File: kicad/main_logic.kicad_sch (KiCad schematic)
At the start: 15 parts, among them U10 74LS00, U17 28 PIN ZIF, U3 74LS245, U4 74LS244, U5 74LS244, U8 74LS04, U9 74LS08

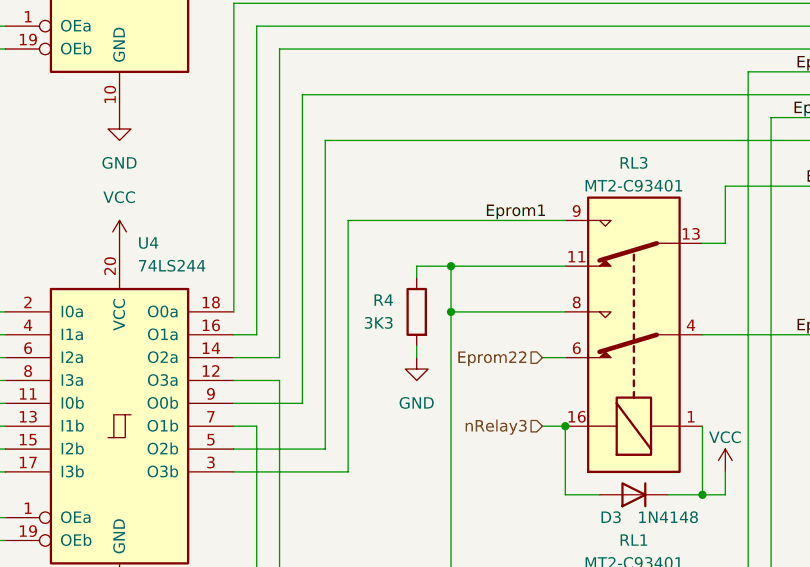
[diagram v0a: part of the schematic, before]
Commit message: KiCAD: larger footprint for 1W resistors
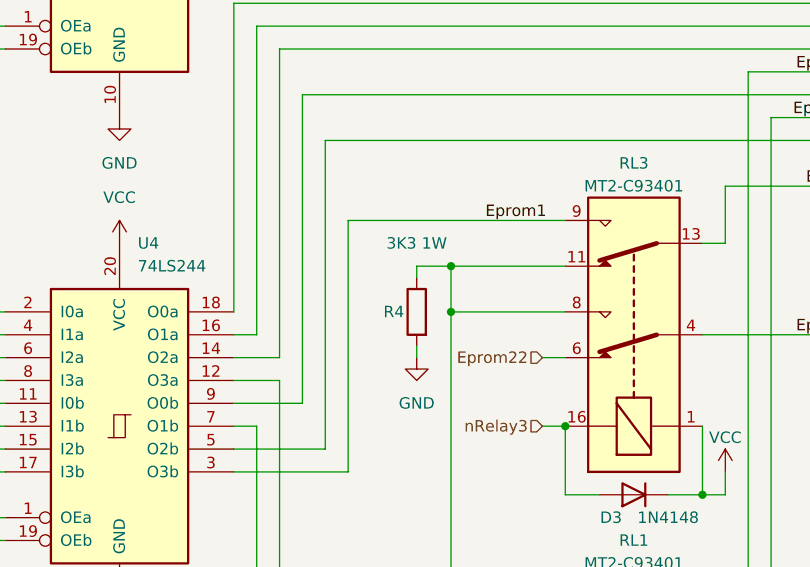
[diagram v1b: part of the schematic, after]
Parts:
- R4: value 3K3 -> 3K3 1W; footprint Resistor_THT:R_Axial_DIN0207_L6.3mm_D2.5mm_P10.16mm_Horizontal -> Resistor_THT:R_Axial_DIN0309_L9.0mm_D3.2mm_P12.70mm_Horizontal
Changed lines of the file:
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@@
   (symbol (lib_id "Device:R") (at 157.48 96.52 0) (mirror y) (unit 1)
     (in_bom yes) (on_board yes)
-    (property "Reference" "R4" (id 0) (at 154.94 95.2499 0)
-      (effects (font (size 1.27 1.27)) (justify left))
-    )
-    (property "Value" "3K3" (id 1) (at 154.94 97.7899 0)
-      (effects (font (size 1.27 1.27)) (justify left))
-    )
-    (property "Footprint" "Resistor_THT:R_Axial_DIN0207_L6.3mm_D2.5mm_P10.16mm_Horizontal" (id 2) (at 159.258 96.52 90)
+    (property "Reference" "R4" (id 0) (at 154.94 96.52 0))
+    (property "Value" "3K3 1W" (id 1) (at 157.48 88.9 0))
+    (property "Footprint" "Resistor_THT:R_Axial_DIN0309_L9.0mm_D3.2mm_P12.70mm_Horizontal" (id 2) (at 159.258 96.52 90)
       (effects (font (size 1.27 1.27)) hide)
     )

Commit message: KiCAD: Make space for full ZIF
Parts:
- R19: footprint custom_footprints:R_Axial_DIN0207_L6.3mm_D2.0mm_P11.43mm_Horizontal -> custom_footprints:R_Axial_DIN0207_L6.3mm_D2.0mm_P10.16mm_Horizontal
- U17: footprint custom_footprints:DIP-28_W15.24mm_Socket_LongPads -> custom_footprints:DIP_Socket-28_W11.9_W12.7_W15.24_W17.78_W18.5_3M_228-1277-00-0602J
- U3, U4, U5: footprint custom_footprints:DIP-20_W7.62mm_Socket -> custom_footprints:DIP-20_W7.62mm_Socket_tweaked
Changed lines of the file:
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@@
       (effects (font (size 1.27 1.27)) (justify left))
     )
-    (property "Footprint" "custom_footprints:DIP-20_W7.62mm_Socket" (id 2) (at 124.46 54.61 0)
+    (property "Footprint" "custom_footprints:DIP-20_W7.62mm_Socket_tweaked" (id 2) (at 124.46 54.61 0)
       (effects (font (size 1.27 1.27)) hide)
     )
@@
       (effects (font (size 1.27 1.27)) (justify left))
     )
-    (property "Footprint" "custom_footprints:DIP-28_W15.24mm_Socket_LongPads" (id 2) (at 222.25 64.77 0)
+    (property "Footprint" "custom_footprints:DIP_Socket-28_W11.9_W12.7_W15.24_W17.78_W18.5_3M_228-1277-00-0602J" (id 2) (at 222.25 64.77 0)
       (effects (font (size 1.27 1.27)) hide)
     )
@@
       (effects (font (size 1.27 1.27)) (justify left))
     )
-    (property "Footprint" "custom_footprints:DIP-20_W7.62mm_Socket" (id 2) (at 256.54 54.61 0)
+    (property "Footprint" "custom_footprints:DIP-20_W7.62mm_Socket_tweaked" (id 2) (at 256.54 54.61 0)
       (effects (font (size 1.27 1.27)) hide)
     )
@@
       (effects (font (size 1.27 1.27)) (justify left))
     )
-    (property "Footprint" "custom_footprints:R_Axial_DIN0207_L6.3mm_D2.0mm_P11.43mm_Horizontal" (id 2) (at 99.822 129.54 90)
+    (property "Footprint" "custom_footprints:R_Axial_DIN0207_L6.3mm_D2.0mm_P10.16mm_Horizontal" (id 2) (at 99.822 129.54 90)
       (effects (font (size 1.27 1.27)) hide)
     )
@@
       (effects (font (size 1.27 1.27)) (justify left))
     )
-    (property "Footprint" "custom_footprints:DIP-20_W7.62mm_Socket" (id 2) (at 124.46 109.22 0)
-      (effects (font (size 1.27 1.27)) hide)
-    )
+    (property "Footprint" "custom_footprints:DIP-20_W7.62mm_Socket_tweaked" (id 2) (at 124.46 109.22 0)
+      (effects (font (size 1.27 1.27)) hide)
+    )

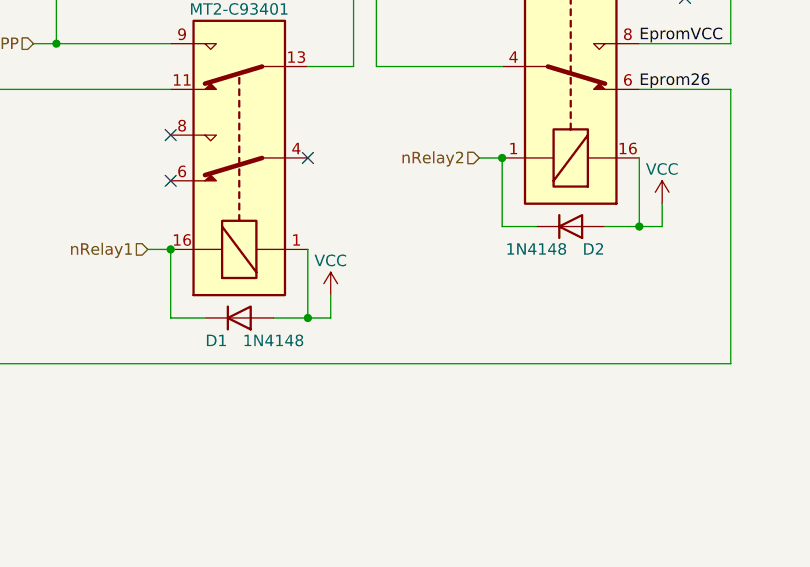
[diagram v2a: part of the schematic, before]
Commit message: KiCAD: Reverse D1/2
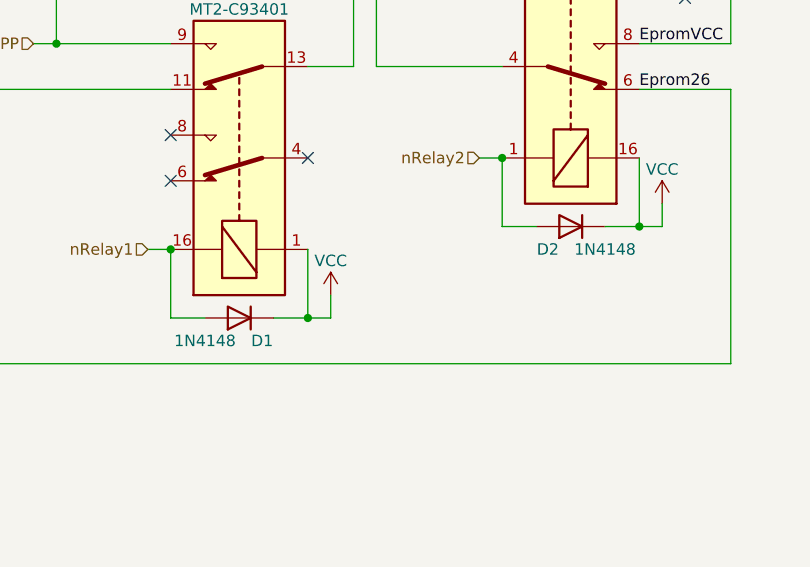
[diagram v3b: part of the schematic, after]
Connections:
- net VCC: now also D1.1 (K), D2.1 (K); no longer D1.2 (A), D2.2 (A)
- net nRelay1: now also D1.2 (A); no longer D1.1 (K)
- net nRelay2: now also D2.2 (A); no longer D2.1 (K)
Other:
- moved on the sheet: D1, D2
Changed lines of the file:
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@@
     (pin "2")
   )
-  (symbol (lib_id "Device:D") (at 218.44 148.59 0) (mirror x) (unit 1)
-    (in_bom yes) (on_board yes)
-    (property "Reference" "D2" (id 0) (at 220.98 151.13 0))
-    (property "Value" "1N4148" (id 1) (at 214.63 151.13 0))
+  (symbol (lib_id "Device:D") (at 218.44 148.59 180) (unit 1)
+    (in_bom yes) (on_board yes)
+    (property "Reference" "D2" (id 0) (at 215.9 151.13 0))
+    (property "Value" "1N4148" (id 1) (at 222.25 151.13 0))
     (property "Footprint" "custom_footprints:D_DO-35_SOD27_P11.43mm_Horizontal" (id 2) (at 218.44 148.59 0)
       (effects (font (size 1.27 1.27)) hide)
@@
     (pin "1")
   )
-  (symbol (lib_id "Device:D") (at 181.61 158.75 0) (mirror x) (unit 1)
-    (in_bom yes) (on_board yes)
-    (property "Reference" "D1" (id 0) (at 179.07 161.29 0))
-    (property "Value" "1N4148" (id 1) (at 185.42 161.29 0))
+  (symbol (lib_id "Device:D") (at 181.61 158.75 180) (unit 1)
+    (in_bom yes) (on_board yes)
+    (property "Reference" "D1" (id 0) (at 184.15 161.29 0))
+    (property "Value" "1N4148" (id 1) (at 177.8 161.29 0))
     (property "Footprint" "custom_footprints:D_DO-35_SOD27_P11.43mm_Horizontal" (id 2) (at 181.61 158.75 0)
       (effects (font (size 1.27 1.27)) hide)
